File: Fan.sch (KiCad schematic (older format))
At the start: 9 parts

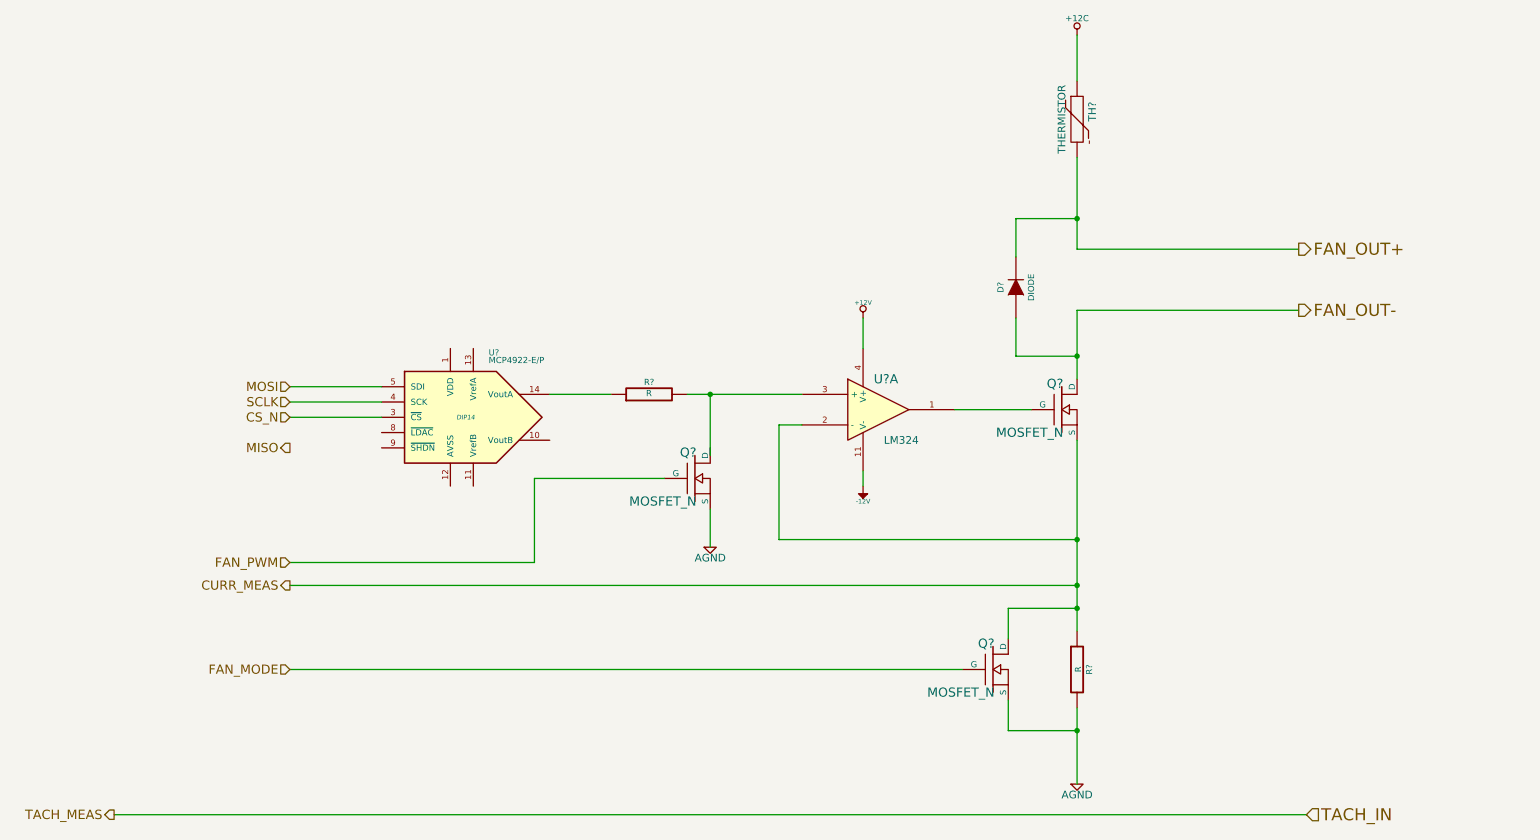
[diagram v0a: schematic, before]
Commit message: Added Relay module footprints.
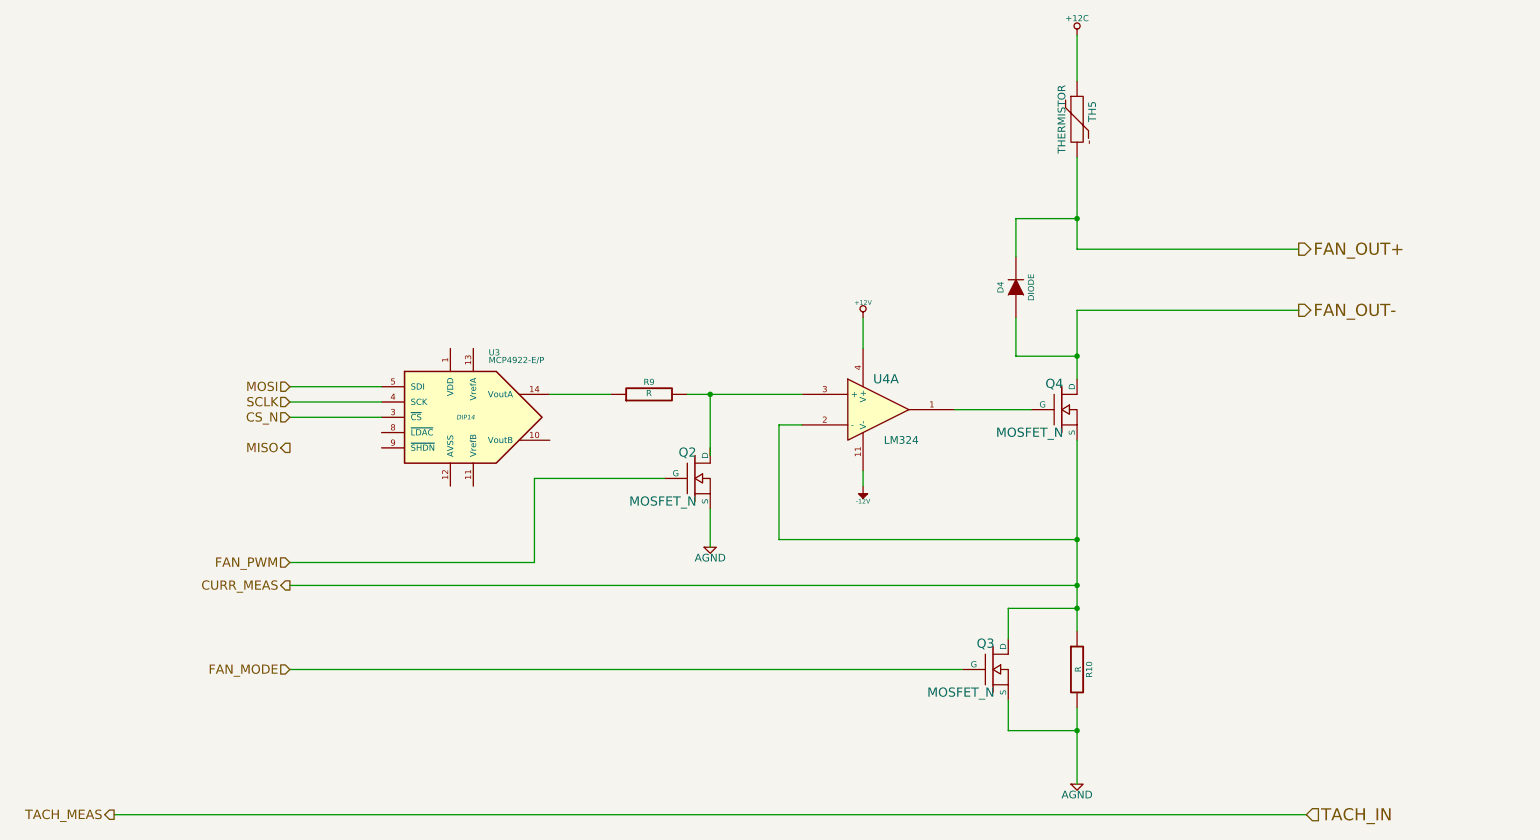
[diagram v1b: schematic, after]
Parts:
- gave numbers to parts that had none: 9
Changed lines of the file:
@@
 LIBS:valves
 LIBS:BB
+LIBS:GLSP
 LIBS:BB-cache
 EELAYER 24 0
@@
 FAN_PWM
 $Comp
-L LM324 U?
+L LM324 U4
 U 1 1 52F62E62
 P 6550 3650
-F 0 "U?" H 6600 3850 60  0000 C CNN
+F 0 "U4" H 6600 3850 60  0000 C CNN
 F 1 "LM324" H 6700 3450 50  0000 C CNN
 F 2 "" H 6550 3650 60  0000 C CNN
@@
 $EndComp
 $Comp
-L MOSFET_N Q?
+L MOSFET_N Q4
 U 1 1 52F62E76
 P 7750 3650
-F 0 "Q?" H 7760 3820 60  0000 R CNN
+F 0 "Q4" H 7760 3820 60  0000 R CNN
 F 1 "MOSFET_N" H 7760 3500 60  0000 R CNN
 F 2 "" H 7750 3650 60  0000 C CNN
@@
 	7050 3650 7550 3650
 $Comp
-L R R?
+L R R10
 U 1 1 52F62EB2
 P 7850 5350
-F 0 "R?" V 7930 5350 40  0000 C CNN
+F 0 "R10" V 7930 5350 40  0000 C CNN
 F 1 "R" V 7857 5351 40  0000 C CNN
 F 2 "" V 7780 5350 30  0000 C CNN
@@
 $EndComp
 $Comp
-L AGND #PWR?
+L AGND #PWR28
 U 1 1 52F62EF1
 P 7850 6100
-F 0 "#PWR?" H 7850 6100 40  0001 C CNN
+F 0 "#PWR28" H 7850 6100 40  0001 C CNN
 F 1 "AGND" H 7850 6030 50  0000 C CNN
 F 2 "" H 7850 6100 60  0000 C CNN
@@
 	5900 3750 6050 3750
 $Comp
-L +12V #PWR?
+L +12V #PWR25
 U 1 1 52F62F17
 P 6450 3050
-F 0 "#PWR?" H 6450 3000 20  0001 C CNN
+F 0 "#PWR25" H 6450 3000 20  0001 C CNN
 F 1 "+12V" H 6450 3150 30  0000 C CNN
 F 2 "" H 6450 3050 60  0000 C CNN
@@
 	6450 3250 6450 3050
 $Comp
-L -12V #PWR?
+L -12V #PWR26
 U 1 1 52F62F30
 P 6450 4150
-F 0 "#PWR?" H 6450 4280 20  0001 C CNN
+F 0 "#PWR26" H 6450 4280 20  0001 C CNN
 F 1 "-12V" H 6450 4250 30  0000 C CNN
 F 2 "" H 6450 4150 60  0000 C CNN
@@
 	6450 4050 6450 4150
 $Comp
-L AGND #PWR?
+L AGND #PWR24
 U 1 1 52F62FD1
 P 5450 4550
-F 0 "#PWR?" H 5450 4550 40  0001 C CNN
+F 0 "#PWR24" H 5450 4550 40  0001 C CNN
 F 1 "AGND" H 5450 4480 50  0000 C CNN
 F 2 "" H 5450 4550 60  0000 C CNN
@@
 	5450 4300 5450 4550
 $Comp
-L MCP4922-E/P U?
+L MCP4922-E/P U3
 U 1 1 52F630F0
 P 3850 3700
-F 0 "U?" H 4000 4100 40  0000 L BNN
+F 0 "U3" H 4000 4100 40  0000 L BNN
 F 1 "MCP4922-E/P" H 4000 4050 40  0000 L BNN
 F 2 "DIP14" H 3850 3700 30  0000 C CIN
@@
 CURR_MEAS
 $Comp
-L R R?
+L R R9
 U 1 1 52F6370A
 P 5050 3550
-F 0 "R?" V 5130 3550 40  0000 C CNN
+F 0 "R9" V 5130 3550 40  0000 C CNN
 F 1 "R" V 5057 3551 40  0000 C CNN
 F 2 "" V 4980 3550 30  0000 C CNN
@@
 	2700 3700 3300 3700
 $Comp
-L MOSFET_N Q?
+L MOSFET_N Q3
 U 1 1 52F95CB1
 P 7300 5350
-F 0 "Q?" H 7310 5520 60  0000 R CNN
+F 0 "Q3" H 7310 5520 60  0000 R CNN
 F 1 "MOSFET_N" H 7310 5200 60  0000 R CNN
 F 2 "" H 7300 5350 60  0000 C CNN
@@
 $EndComp
 $Comp
-L THERMISTOR TH?
+L THERMISTOR TH5
 U 1 1 52F95CC8
 P 7850 1750
-F 0 "TH?" V 7950 1800 50  0000 C CNN
+F 0 "TH5" V 7950 1800 50  0000 C CNN
 F 1 "THERMISTOR" V 7750 1750 50  0000 C CNN
 F 2 "" H 7850 1750 60  0000 C CNN
@@
 	7850 3000 9300 3000
 $Comp
-L DIODE D?
+L DIODE D4
 U 1 1 52F95D3D
 P 7450 2850
-F 0 "D?" H 7450 2950 40  0000 C CNN
+F 0 "D4" H 7450 2950 40  0000 C CNN
 F 1 "DIODE" H 7450 2750 40  0000 C CNN
 F 2 "" H 7450 2850 60  0000 C CNN
@@
 	2700 4650 4300 4650
 $Comp
-L MOSFET_N Q?
+L MOSFET_N Q2
 U 1 1 52F95F21
 P 5350 4100
-F 0 "Q?" H 5360 4270 60  0000 R CNN
+F 0 "Q2" H 5360 4270 60  0000 R CNN
 F 1 "MOSFET_N" H 5360 3950 60  0000 R CNN
 F 2 "" H 5350 4100 60  0000 C CNN
@@
 FAN_MODE
 $Comp
-L +12C #PWR?
+L +12C #PWR27
 U 1 1 52F96856
 P 7850 1200
-F 0 "#PWR?" H 7850 1170 30  0001 C CNN
+F 0 "#PWR27" H 7850 1170 30  0001 C CNN
 F 1 "+12C" H 7850 1310 40  0000 C CNN
 F 2 "" H 7850 1200 60  0000 C CNN

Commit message: Associated and placed thermocouple, terminal, arduino, fan driver, power protection modules.
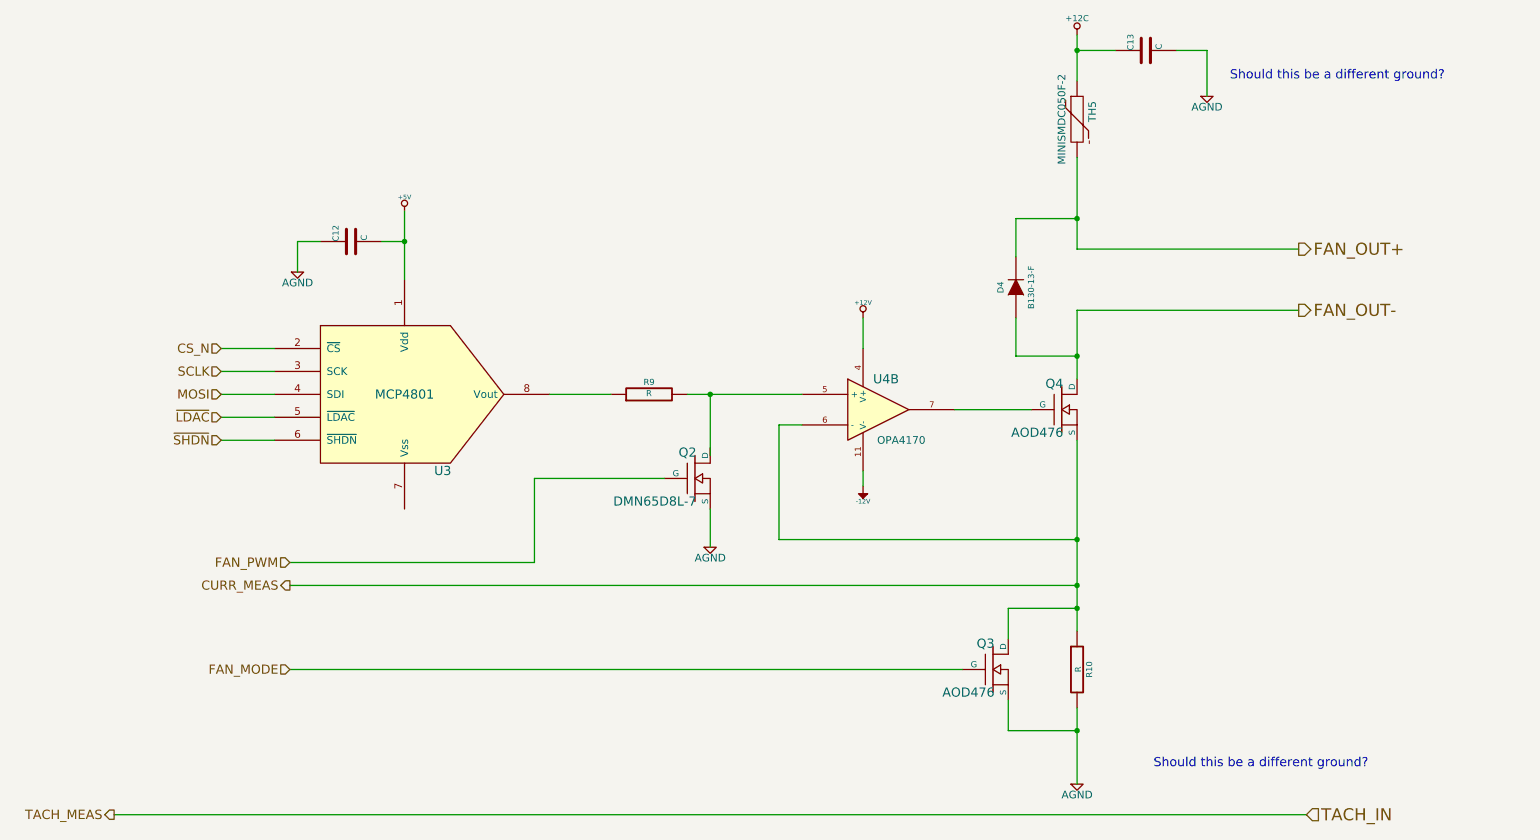
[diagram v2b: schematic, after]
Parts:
- removed Q3, Q4: MOSFET_N, symbol MOSFET_N
- removed U3: MCP4922-E/P, DIP14, symbol MCP4922-E/P
- added C12, C13: C, symbol C
- added Q3, Q4: AOD476, symbol MOS_N_NUM
- added U3: MCP4801, symbol MCP4801
- D4: value DIODE -> B130-13-F; MFG Part Number (none) -> B130-13-F; MFG name (none) -> Diodes Inc
- Q2: value MOSFET_N -> DMN65D8L-7; MFG Part Number (none) -> DMN65D8L-7; MFG name (none) -> Diodes Inc
- TH5: value THERMISTOR -> MINISMDC050F-2; MFG Part Number (none) -> MINISMDC050F-2; MFG name (none) -> TE Connectivity
- U4: value LM324 -> OPA4170
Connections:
- net +12C: now also C13.1
- net AGND: now also C12.1, C13.2, Q3.3 (S)
- net CS_N: now also U3.2 (~CS)
- net CURR_MEAS: now also U4.6 (-), Q3.2 (D), Q4.3 (S); no longer U4.2 (-)
- net FAN_MODE: now also Q3.1 (G)
- net FAN_OUT-: now also Q4.2 (D)
- net MOSI: now also U3.4 (SDI)
- net SCLK: now also U3.3 (SCK)
- net at R9.2: now also U4.5 (+); no longer U4.3 (+)
- net at R9.1: now also U3.8 (Vout)
- new net: Q4.1 (G), U4.7
- new net +5V: C12.2, U3.1 (Vdd)
- new net ~LDAC: U3.5 (~LDAC)
- new net ~SHDN: U3.6 (~SHDN)
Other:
- note added: "Should this be a different ground?"
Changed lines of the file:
@@
 $Descr A4 11693 8268
 encoding utf-8
-Sheet 5 9
+Sheet 9 9
 Title ""
 Date ""
@@
 $Comp
 L LM324 U4
-U 1 1 52F62E62
+U 2 1 52F62E62
 P 6550 3650
 F 0 "U4" H 6600 3850 60  0000 C CNN
-F 1 "LM324" H 6700 3450 50  0000 C CNN
+F 1 "OPA4170" H 6700 3450 50  0000 C CNN
 F 2 "" H 6550 3650 60  0000 C CNN
 F 3 "" H 6550 3650 60  0000 C CNN
-	1    6550 3650
-	1    0    0    -1
-$EndComp
-$Comp
-L MOSFET_N Q4
-U 1 1 52F62E76
-P 7750 3650
-F 0 "Q4" H 7760 3820 60  0000 R CNN
-F 1 "MOSFET_N" H 7760 3500 60  0000 R CNN
-F 2 "" H 7750 3650 60  0000 C CNN
-F 3 "" H 7750 3650 60  0000 C CNN
-	1    7750 3650
+	2    6550 3650
 	1    0    0    -1
 $EndComp
@@
 $EndComp
 $Comp
-L AGND #PWR28
+L AGND #PWR059
 U 1 1 52F62EF1
 P 7850 6100
-F 0 "#PWR28" H 7850 6100 40  0001 C CNN
+F 0 "#PWR059" H 7850 6100 40  0001 C CNN
 F 1 "AGND" H 7850 6030 50  0000 C CNN
 F 2 "" H 7850 6100 60  0000 C CNN
@@
 	5900 3750 6050 3750
 $Comp
-L +12V #PWR25
+L +12V #PWR060
 U 1 1 52F62F17
 P 6450 3050
-F 0 "#PWR25" H 6450 3000 20  0001 C CNN
+F 0 "#PWR060" H 6450 3000 20  0001 C CNN
 F 1 "+12V" H 6450 3150 30  0000 C CNN
 F 2 "" H 6450 3050 60  0000 C CNN
@@
 	6450 3250 6450 3050
 $Comp
-L -12V #PWR26
+L -12V #PWR061
 U 1 1 52F62F30
 P 6450 4150
-F 0 "#PWR26" H 6450 4280 20  0001 C CNN
+F 0 "#PWR061" H 6450 4280 20  0001 C CNN
 F 1 "-12V" H 6450 4250 30  0000 C CNN
 F 2 "" H 6450 4150 60  0000 C CNN
@@
 	6450 4050 6450 4150
 $Comp
-L AGND #PWR24
+L AGND #PWR062
 U 1 1 52F62FD1
 P 5450 4550
-F 0 "#PWR24" H 5450 4550 40  0001 C CNN
+F 0 "#PWR062" H 5450 4550 40  0001 C CNN
 F 1 "AGND" H 5450 4480 50  0000 C CNN
 F 2 "" H 5450 4550 60  0000 C CNN
@@
 Wire Wire Line
 	5450 4300 5450 4550
-$Comp
-L MCP4922-E/P U3
-U 1 1 52F630F0
-P 3850 3700
-F 0 "U3" H 4000 4100 40  0000 L BNN
-F 1 "MCP4922-E/P" H 4000 4050 40  0000 L BNN
-F 2 "DIP14" H 3850 3700 30  0000 C CIN
-F 3 "" H 3850 3700 60  0000 C CNN
-	1    3850 3700
-	1    0    0    -1
-$EndComp
 Text HLabel 2700 4800 0    60   Output ~ 0
 CURR_MEAS
@@
 Wire Wire Line
 	4400 3550 4800 3550
-Text HLabel 2700 3600 0    60   Input ~ 0
+Text HLabel 2250 3400 0    60   Input ~ 0
 SCLK
-Text HLabel 2700 3700 0    60   Input ~ 0
+Text HLabel 2250 3250 0    60   Input ~ 0
 CS_N
-Text HLabel 2700 3500 0    60   Input ~ 0
+Text HLabel 2250 3550 0    60   Input ~ 0
 MOSI
-Text HLabel 2700 3900 0    60   Output ~ 0
-MISO
-Wire Wire Line
-	2700 3500 3300 3500
-Wire Wire Line
-	2700 3600 3300 3600
-Wire Wire Line
-	2700 3700 3300 3700
-$Comp
-L MOSFET_N Q3
-U 1 1 52F95CB1
-P 7300 5350
-F 0 "Q3" H 7310 5520 60  0000 R CNN
-F 1 "MOSFET_N" H 7310 5200 60  0000 R CNN
-F 2 "" H 7300 5350 60  0000 C CNN
-F 3 "" H 7300 5350 60  0000 C CNN
-	1    7300 5350
-	1    0    0    -1
-$EndComp
 $Comp
 L THERMISTOR TH5
@@
 P 7850 1750
 F 0 "TH5" V 7950 1800 50  0000 C CNN
-F 1 "THERMISTOR" V 7750 1750 50  0000 C CNN
+F 1 "MINISMDC050F-2" V 7750 1750 50  0000 C CNN
 F 2 "" H 7850 1750 60  0000 C CNN
 F 3 "" H 7850 1750 60  0000 C CNN
+F 4 "TE Connectivity" H 7850 1750 60  0001 C CNN "MFG name"
+F 5 "MINISMDC050F-2" H 7850 1750 60  0001 C CNN "MFG Part Number"
 	1    7850 1750
 	1    0    0    -1
@@
 P 7450 2850
 F 0 "D4" H 7450 2950 40  0000 C CNN
-F 1 "DIODE" H 7450 2750 40  0000 C CNN
+F 1 "B130-13-F" H 7450 2750 40  0000 C CNN
 F 2 "" H 7450 2850 60  0000 C CNN
 F 3 "" H 7450 2850 60  0000 C CNN
+F 4 "Diodes Inc" H 7450 2850 60  0001 C CNN "MFG name"
+F 5 "B130-13-F" H 7450 2850 60  0001 C CNN "MFG Part Number"
 	1    7450 2850
 	0    -1   -1   0
@@
 P 5350 4100
 F 0 "Q2" H 5360 4270 60  0000 R CNN
-F 1 "MOSFET_N" H 5360 3950 60  0000 R CNN
+F 1 "DMN65D8L-7" H 5360 3950 60  0000 R CNN
 F 2 "" H 5350 4100 60  0000 C CNN
 F 3 "" H 5350 4100 60  0000 C CNN
+F 4 "Diodes Inc" H 5350 4100 60  0001 C CNN "MFG name"
+F 5 "DMN65D8L-7" H 5350 4100 60  0001 C CNN "MFG Part Number"
 	1    5350 4100
 	1    0    0    -1
@@
 FAN_MODE
 $Comp
-L +12C #PWR27
+L +12C #PWR063
 U 1 1 52F96856
 P 7850 1200
-F 0 "#PWR27" H 7850 1170 30  0001 C CNN
+F 0 "#PWR063" H 7850 1170 30  0001 C CNN
 F 1 "+12C" H 7850 1310 40  0000 C CNN
 F 2 "" H 7850 1200 60  0000 C CNN
@@
 	1    0    0    -1
 $EndComp
+Wire Wire Line
+	2600 3250 2250 3250
+Wire Wire Line
+	2600 3400 2250 3400
+Wire Wire Line
+	2250 3550 2600 3550
+$Comp
+L MCP4801 U3
+U 1 1 530A3BD3
+P 3450 3550
+F 0 "U3" H 3700 3050 60  0000 C CNN
+F 1 "MCP4801" H 3450 3550 60  0000 C CNN
+F 2 "" H 3450 3550 60  0000 C CNN
+F 3 "" H 3450 3550 60  0000 C CNN
+	1    3450 3550
+	1    0    0    -1
+$EndComp
+Text HLabel 2250 3700 0    60   Input ~ 0
+~LDAC
+Text HLabel 2250 3850 0    60   Input ~ 0
+~SHDN
+Wire Wire Line
+	2250 3700 2600 3700
+Wire Wire Line
+	2600 3850 2250 3850
+$Comp
+L C C12
+U 1 1 530AD6D7
+P 3100 2550
+F 0 "C12" H 3100 2650 40  0000 L CNN
+F 1 "C" H 3106 2465 40  0000 L CNN
+F 2 "" H 3138 2400 30  0000 C CNN
+F 3 "" H 3100 2550 60  0000 C CNN
+	1    3100 2550
+	0    -1   -1   0
+$EndComp
+$Comp
+L AGND #PWR064
+U 1 1 530AD6DD
+P 2750 2750
+F 0 "#PWR064" H 2750 2750 40  0001 C CNN
+F 1 "AGND" H 2750 2680 50  0000 C CNN
+F 2 "" H 2750 2750 60  0000 C CNN
+F 3 "" H 2750 2750 60  0000 C CNN
+	1    2750 2750
+	1    0    0    -1
+$EndComp
+$Comp
+L +5V #PWR065
+U 1 1 530AD6E3
+P 3450 2350
+F 0 "#PWR065" H 3450 2440 20  0001 C CNN
+F 1 "+5V" H 3450 2440 30  0000 C CNN
+F 2 "" H 3450 2350 60  0000 C CNN
+F 3 "" H 3450 2350 60  0000 C CNN
+	1    3450 2350
+	1    0    0    -1
+$EndComp
+Wire Wire Line
+	3450 2350 3450 2800
+Wire Wire Line
+	3300 2550 3450 2550
+Connection ~ 3450 2550
+Wire Wire Line
+	2900 2550 2750 2550
+Wire Wire Line
+	2750 2550 2750 2750
+$Comp
+L C C13
+U 1 1 530A4A2B
+P 8300 1300
+F 0 "C13" H 8300 1400 40  0000 L CNN
+F 1 "C" H 8306 1215 40  0000 L CNN
+F 2 "" H 8338 1150 30  0000 C CNN
+F 3 "" H 8300 1300 60  0000 C CNN
+	1    8300 1300
+	0    -1   -1   0
+$EndComp
+$Comp
+L AGND #PWR066
+U 1 1 530A4A36
+P 8700 1600
+F 0 "#PWR066" H 8700 1600 40  0001 C CNN
+F 1 "AGND" H 8700 1530 50  0000 C CNN
+F 2 "" H 8700 1600 60  0000 C CNN
+F 3 "" H 8700 1600 60  0000 C CNN
+	1    8700 1600
+	1    0    0    -1
+$EndComp
+Wire Wire Line
+	8100 1300 7850 1300
+Connection ~ 7850 1300
+Wire Wire Line
+	8500 1300 8700 1300
+Wire Wire Line
+	8700 1300 8700 1600
+Text Notes 8850 1500 0    60   ~ 0
+Should this be a different ground?
+Text Notes 8350 6000 0    60   ~ 0
+Should this be a different ground?
+$Comp
+L MOS_N_NUM Q3
+U 1 1 530A4E79
+P 7300 5350
+F 0 "Q3" H 7310 5520 60  0000 R CNN
+F 1 "AOD476" H 7310 5200 60  0000 R CNN
+F 2 "" H 7300 5350 60  0000 C CNN
+F 3 "" H 7300 5350 60  0000 C CNN
+F 4 "AOD476" H 7300 5350 60  0001 C CNN "MFG Part Number"
+	1    7300 5350
+	1    0    0    -1
+$EndComp
+$Comp
+L MOS_N_NUM Q4
+U 1 1 530A4EBB
+P 7750 3650
+F 0 "Q4" H 7760 3820 60  0000 R CNN
+F 1 "AOD476" H 7760 3500 60  0000 R CNN
+F 2 "" H 7750 3650 60  0000 C CNN
+F 3 "" H 7750 3650 60  0000 C CNN
+F 4 "AOD476" H 7750 3650 60  0001 C CNN "MFG Part Number"
+	1    7750 3650
+	1    0    0    -1
+$EndComp
